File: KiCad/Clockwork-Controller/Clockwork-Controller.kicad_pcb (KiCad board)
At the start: 2 copper layers, 56.4 x 94.2 mm, 98 parts, among them CN2 PJ-307N5, J2 to DIN-6 Male, J3 Pause Button, J4 ICSP, J5 LED-Connector, J6 FTDI, Q1 AO3400A, Q2 SS8050, Q3 SS8050, Q4 SS8050, SW1 Guide/Follow, SW2 Mode -, SW3 Mode +, SW4 Frame -, SW5 Frame +, U1 ECS-TXO-3225MV-160-TR, U2 AP2210N-3.3TRG1, U3 74HCT14, U4 G3VM-61VY3(TR), U5 MCP4725, U6 LMC6482, U7 ATmega328P-A

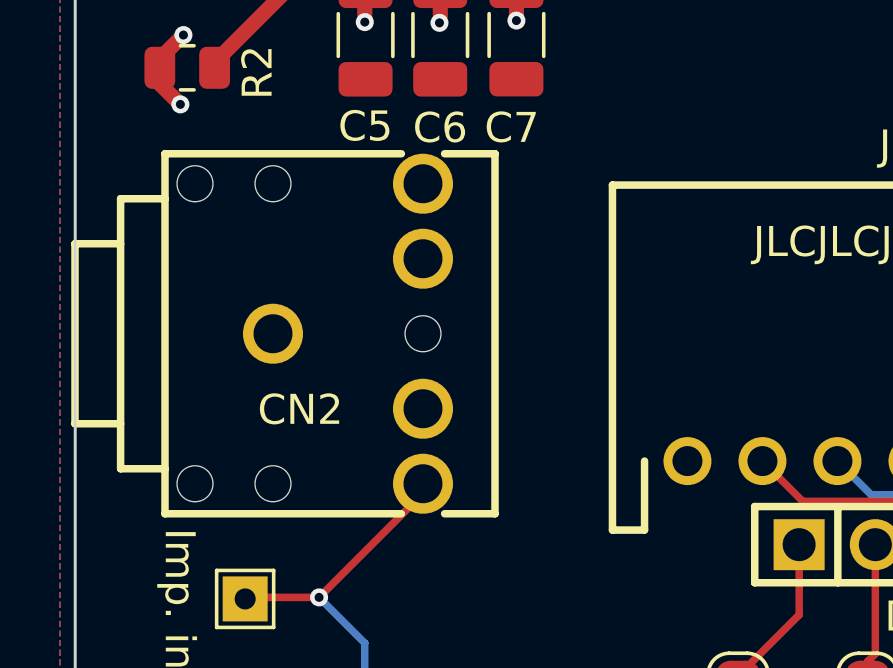
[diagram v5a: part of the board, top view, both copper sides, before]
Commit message: Using both left and right channel for ESS in
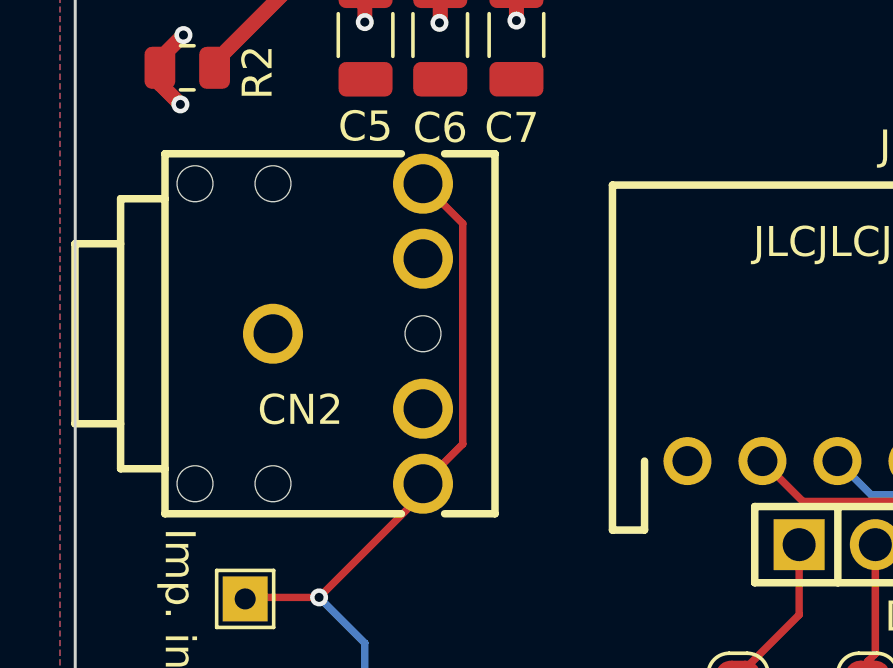
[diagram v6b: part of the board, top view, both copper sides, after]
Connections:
- CN2 pad 3: unconnected-(CN2-Pad3) -> Net-(CN2-Pad2)
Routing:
- net Net-(CN2-Pad2): track 31.4 -> 42.5 mm
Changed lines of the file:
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@@
 	(net 66 "unconnected-(SW1-Pad4)")
 	(net 67 "unconnected-(SW1-Pad5)")
-	(net 68 "unconnected-(CN2-Pad3)")
-	(net 69 "Net-(CN2-Pad2)")
-	(net 70 "/DTR")
+	(net 68 "Net-(CN2-Pad2)")
+	(net 69 "/DTR")
 	(footprint "Capacitor_SMD:C_0603_1608Metric"
 		(layer "F.Cu")
@@
 			(layers "*.Cu" "*.Mask")
 			(remove_unused_layers no)
-			(net 69 "Net-(CN2-Pad2)")
+			(net 68 "Net-(CN2-Pad2)")
 			(pinfunction "2")
 			(pintype "output")
@@
 			(layers "*.Cu" "*.Mask")
 			(remove_unused_layers no)
-			(net 68 "unconnected-(CN2-Pad3)")
+			(net 68 "Net-(CN2-Pad2)")
 			(pinfunction "3")
-			(pintype "passive+no_connect")
+			(pintype "passive")
 		)
 		(pad "4" thru_hole circle
@@
 			(layers "F.Cu" "F.Paste" "F.Mask")
 			(roundrect_rratio 0.25)
-			(net 70 "/DTR")
+			(net 69 "/DTR")
 			(pintype "passive")
 		)
@@
 			(layers "*.Cu" "*.Mask")
 			(remove_unused_layers no)
-			(net 69 "Net-(CN2-Pad2)")
+			(net 68 "Net-(CN2-Pad2)")
 			(pinfunction "1")
 			(pintype "passive")
@@
 			(layers "F.Cu" "F.Paste" "F.Mask")
 			(roundrect_rratio 0.25)
-			(net 69 "Net-(CN2-Pad2)")
+			(net 68 "Net-(CN2-Pad2)")
 			(pintype "passive")
 		)
@@
 			(layers "*.Cu" "*.Mask")
 			(remove_unused_layers no)
-			(net 70 "/DTR")
+			(net 69 "/DTR")
 			(pinfunction "Pin_6")
 			(pintype "passive")
@@
 	)
 	(segment
+		(start 50.2 34.37)
+		(end 51.525 35.695)
+		(width 0.25)
+		(layer "F.Cu")
+		(net 68)
+	)
+	(segment
+		(start 51.525 35.695)
+		(end 51.525 43.045)
+		(width 0.25)
+		(layer "F.Cu")
+		(net 68)
+	)
+	(segment
 		(start 47.498 69.342)
 		(end 47.498 69.7195)
 		(width 0.25)
 		(layer "F.Cu")
-		(net 69)
+		(net 68)
 	)
 	(segment
@@
 		(width 0.25)
 		(layer "F.Cu")
-		(net 69)
+		(net 68)
 	)
 	(segment
@@
 		(width 0.25)
 		(layer "F.Cu")
-		(net 69)
+		(net 68)
 	)
 	(segment
@@
 		(width 0.25)
 		(layer "F.Cu")
-		(net 69)
+		(net 68)
+	)
+	(segment
+		(start 51.525 43.045)
+		(end 50.2 44.37)
+		(width 0.25)
+		(layer "F.Cu")
+		(net 68)
 	)
 	(segment
@@
 		(width 0.25)
 		(layer "F.Cu")
-		(net 69)
+		(net 68)
 	)
 	(segment
@@
 		(width 0.25)
 		(layer "F.Cu")
-		(net 69)
+		(net 68)
 	)
 	(segment
@@
 		(width 0.25)
 		(layer "F.Cu")
-		(net 69)
+		(net 68)
 	)
 	(via
@@
 		(drill 0.3)
 		(layers "F.Cu" "B.Cu")
-		(net 69)
+		(net 68)
 	)
 	(via
@@
 		(drill 0.3)
 		(layers "F.Cu" "B.Cu")
-		(net 69)
+		(net 68)
 	)
 	(segment
@@
 		(width 0.25)
 		(layer "B.Cu")
-		(net 69)
+		(net 68)
 	)
 	(segment
@@
 		(width 0.25)
 		(layer "B.Cu")
-		(net 69)
+		(net 68)
 	)
 	(segment
@@
 		(width 0.25)
 		(layer "B.Cu")
-		(net 69)
+		(net 68)
 	)
 	(segment
@@
 		(width 0.25)
 		(layer "F.Cu")
-		(net 70)
+		(net 69)
 	)
 	(segment
@@
 		(width 0.25)
 		(layer "F.Cu")
-		(net 70)
+		(net 69)
 	)
 	(segment
@@
 		(width 0.25)
 		(layer "F.Cu")
-		(net 70)
+		(net 69)
 	)
 	(segment
@@
 		(width 0.25)
 		(layer "F.Cu")
-		(net 70)
+		(net 69)
 	)
 	(zone

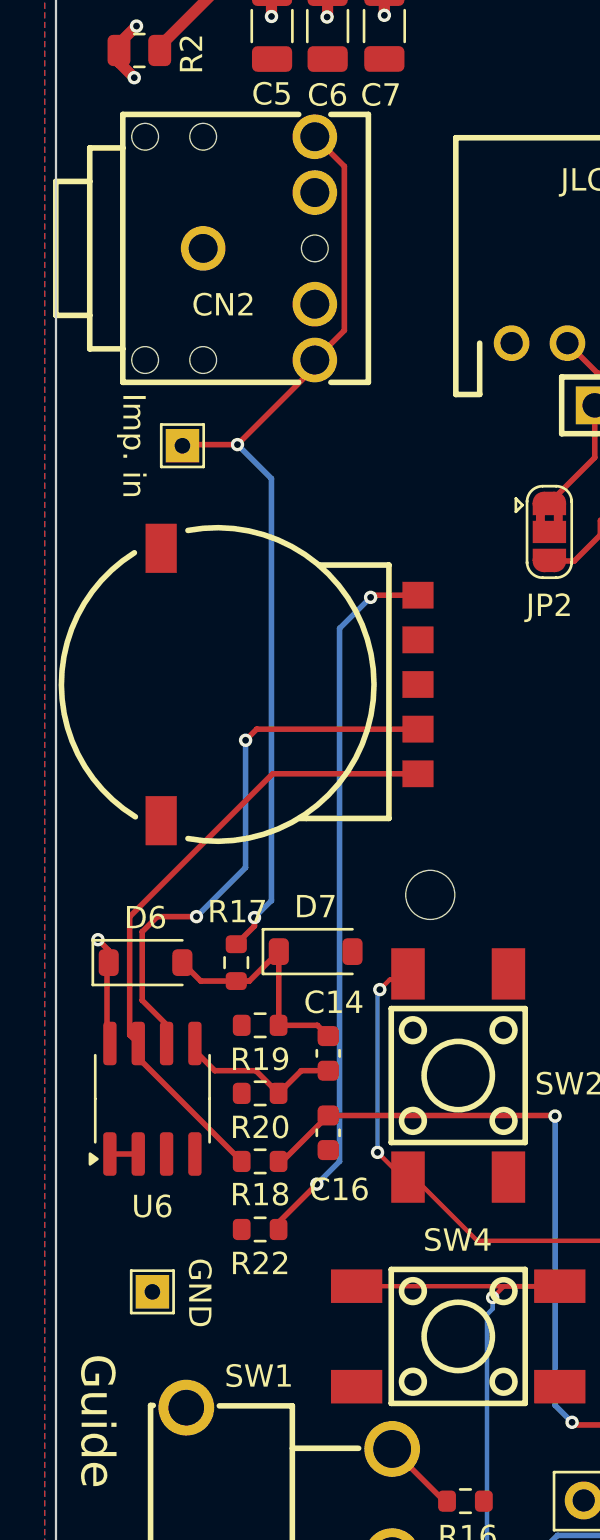
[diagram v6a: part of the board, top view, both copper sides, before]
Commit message: Properly summing up R and L channel using the second OpAmp
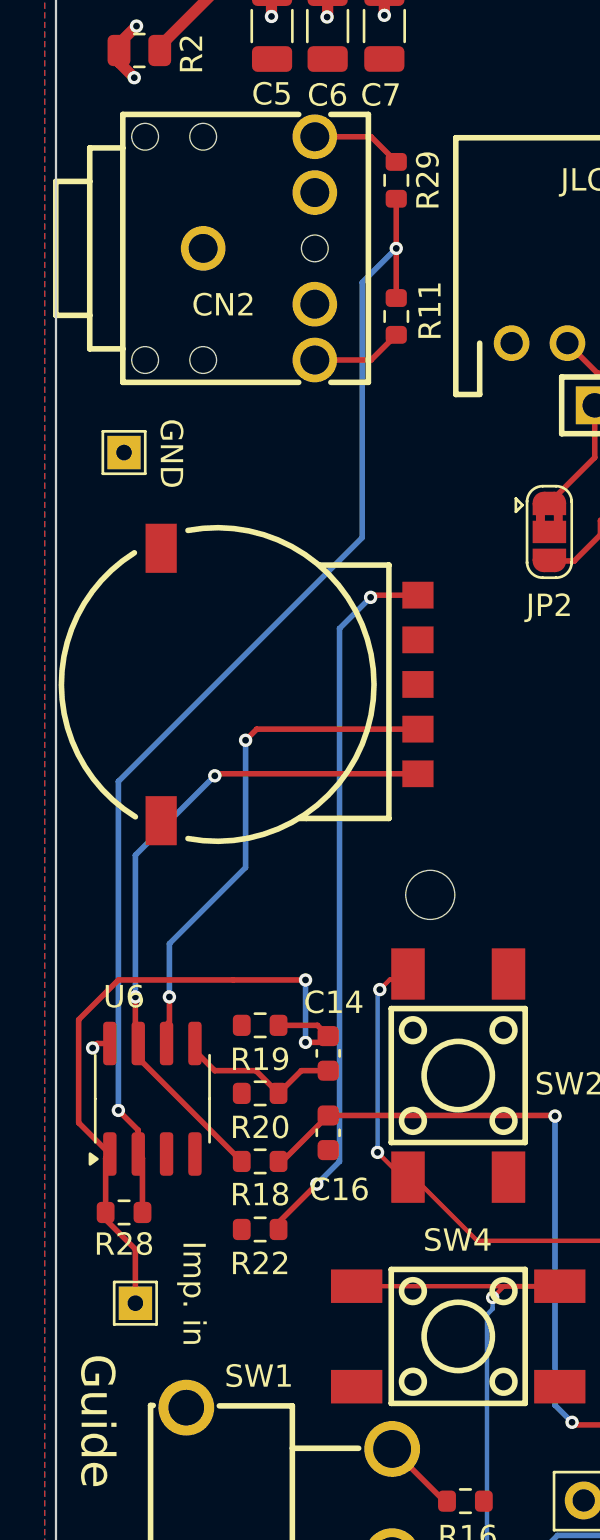
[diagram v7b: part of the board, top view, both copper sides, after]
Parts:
- removed D6, D7: B5819W SL, Diode_SMD:D_SOD-123
- removed R17: 10k, Resistor_SMD:R_0603_1608Metric
- added R11: 10k, Resistor_SMD:R_0603_1608Metric, F.Cu at (53.8, 42.4)
- added R28: 22k, Resistor_SMD:R_0603_1608Metric, F.Cu at (41.7, 82.5)
- added R29: 10k, Resistor_SMD:R_0603_1608Metric, F.Cu at (53.8, 36.3)
- moved TP9 38.5 mm to (42.2, 86.6)
- moved TP3 37.6 mm to (41.7, 48.5)
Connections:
- C14 pad 1: Net-(D6-A) -> Net-(C14-Pad1)
- CN2 pad 3: Net-(CN2-Pad2) -> Net-(CN2-Pad3)
- R19 pad 2: Net-(D6-A) -> Net-(C14-Pad1)
- TP9 pad 1: Net-(CN2-Pad2) -> Net-(C14-Pad1)
- U6 pad 1: Net-(U6A--) -> Net-(C14-Pad1)
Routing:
- net Net-(U6A--): track 1.27 -> 53.2 mm, vias 0 -> 2
- net Net-(CN2-Pad2): track 42.5 -> 4.11 mm, vias 2 -> 0
- net Net-(C14-Pad1): track 0.00 -> 31.2 mm, vias 0 -> 2
- net Net-(D6-A): track 10.9 -> 0.00 mm
- net Net-(CN2-Pad3): track 0.00 -> 4.11 mm
- net +5V: track 64.6 -> 60.5 mm
- net Net-(U6B--): track 24.9 -> 23.0 mm
- net Net-(R18-Pad1): track 28.6 -> 29.9 mm, vias 0 -> 2
